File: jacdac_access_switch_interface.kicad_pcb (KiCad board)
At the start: 2 copper layers, 25 x 25 mm, 23 parts, among them J1 Conn_Jacdac_CardEdge, J2 54-00036_audio_plug, J3 Conn_HackConnect, U1 NCP114ASN330T1G, U2 STM32G031J6M6, U3 AQY282

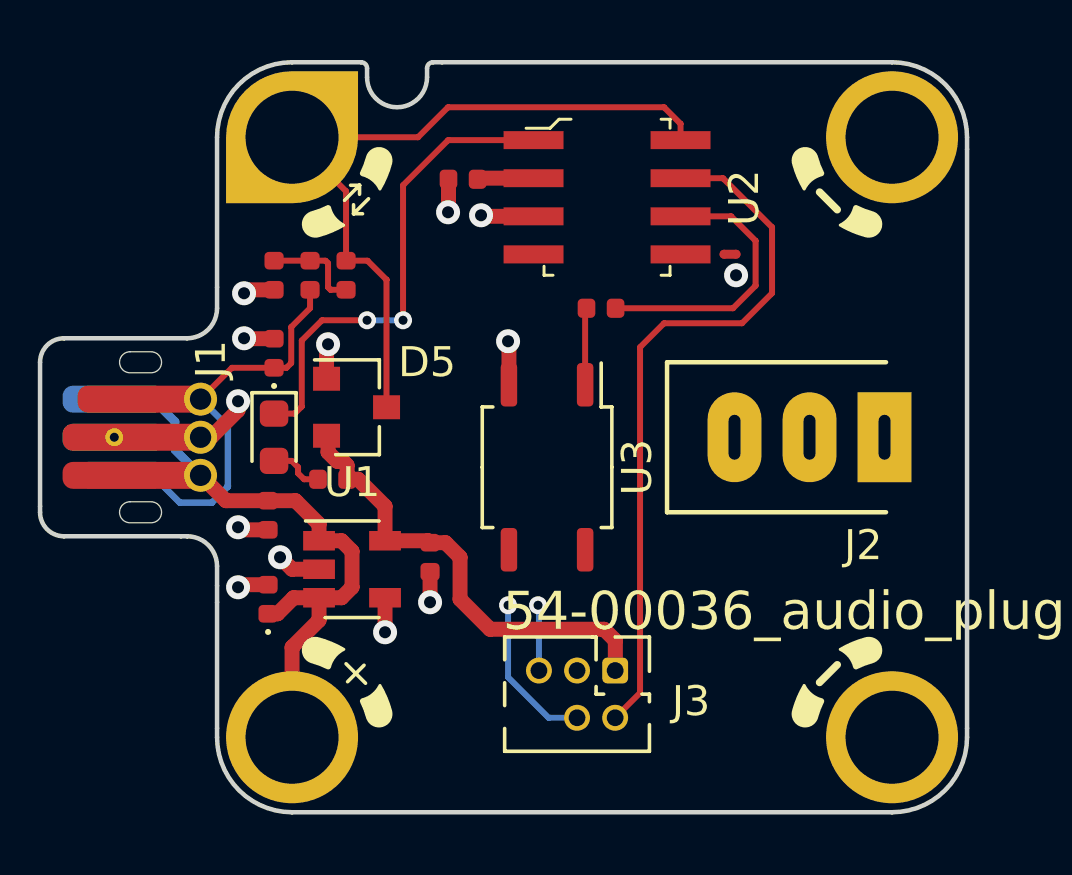
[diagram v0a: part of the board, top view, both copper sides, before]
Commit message: Added 3dshapes and updated PCB
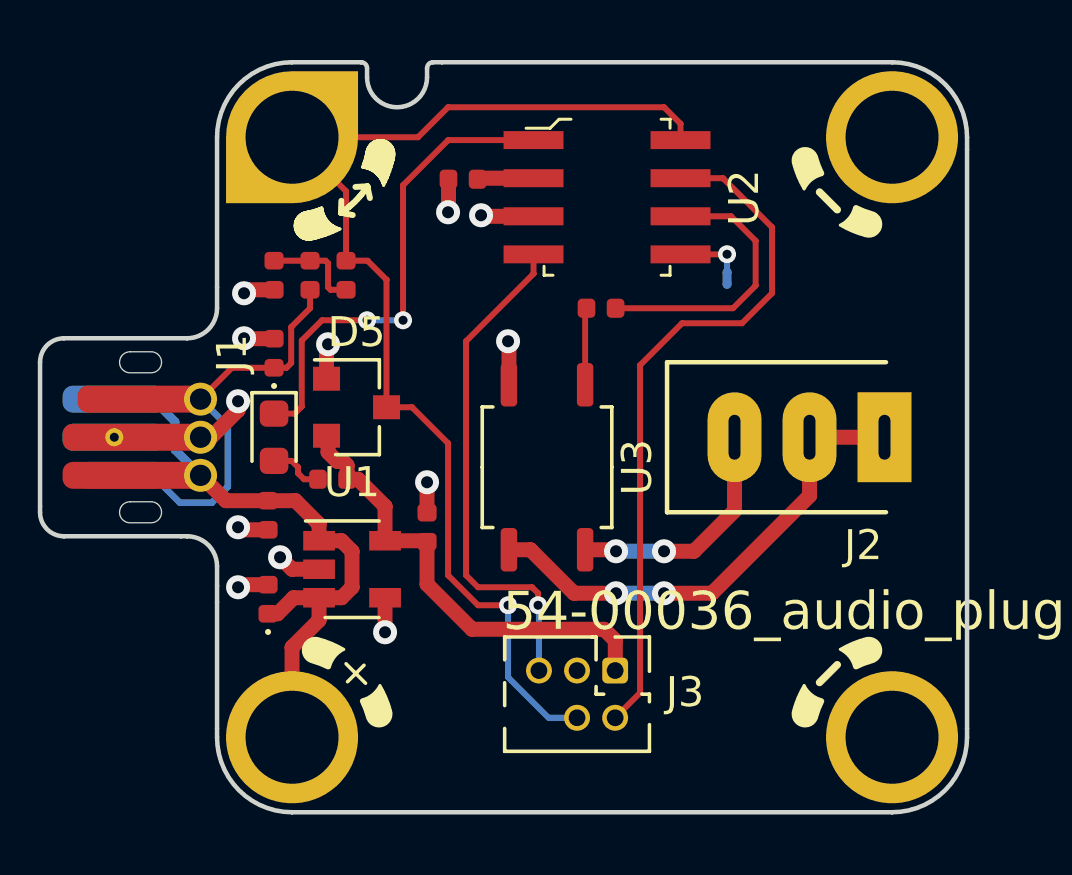
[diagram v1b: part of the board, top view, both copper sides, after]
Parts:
- NT1: moved to B.Cu
- U3: footprint Package_SO:SOP-4_3.8x4.1mm_P2.54mm -> jacdac_access_switch_interface:SOP-4_3.8x4.1mm_P2.54mm
- moved C4 1.00 mm to (154.5, 93.0), turned to 90 degrees
- moved NT1 0.81 mm to (164.5, 84.7), turned to 90 degrees
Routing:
- net /SLEEVE: track 0.00 -> 16.4 mm, vias 0 -> 2
- net /nRESET: track 2.19 -> 16.9 mm
- net /JD_DATA_MCU_SWCLK: track 30.1 -> 39.5 mm
- net /PLUG_TIP: track 0.00 -> 8.30 mm, vias 0 -> 2
- net Net-(U2-PA8/PA11[PA9]/PB0/PB1): track 0.00 -> 2.15 mm, vias 0 -> 1
- net GND: vias 13 -> 12

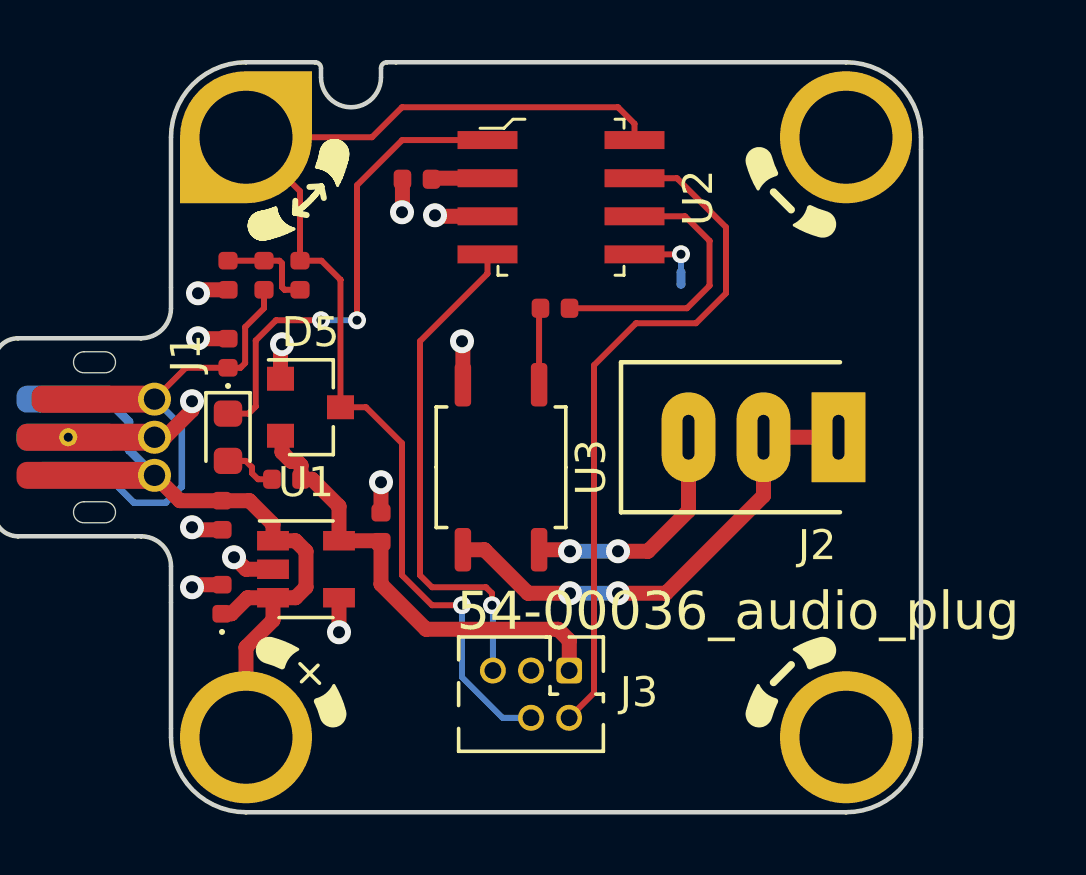
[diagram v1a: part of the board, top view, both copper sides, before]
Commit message: v1.2 almost routed. Found error in connector placement.
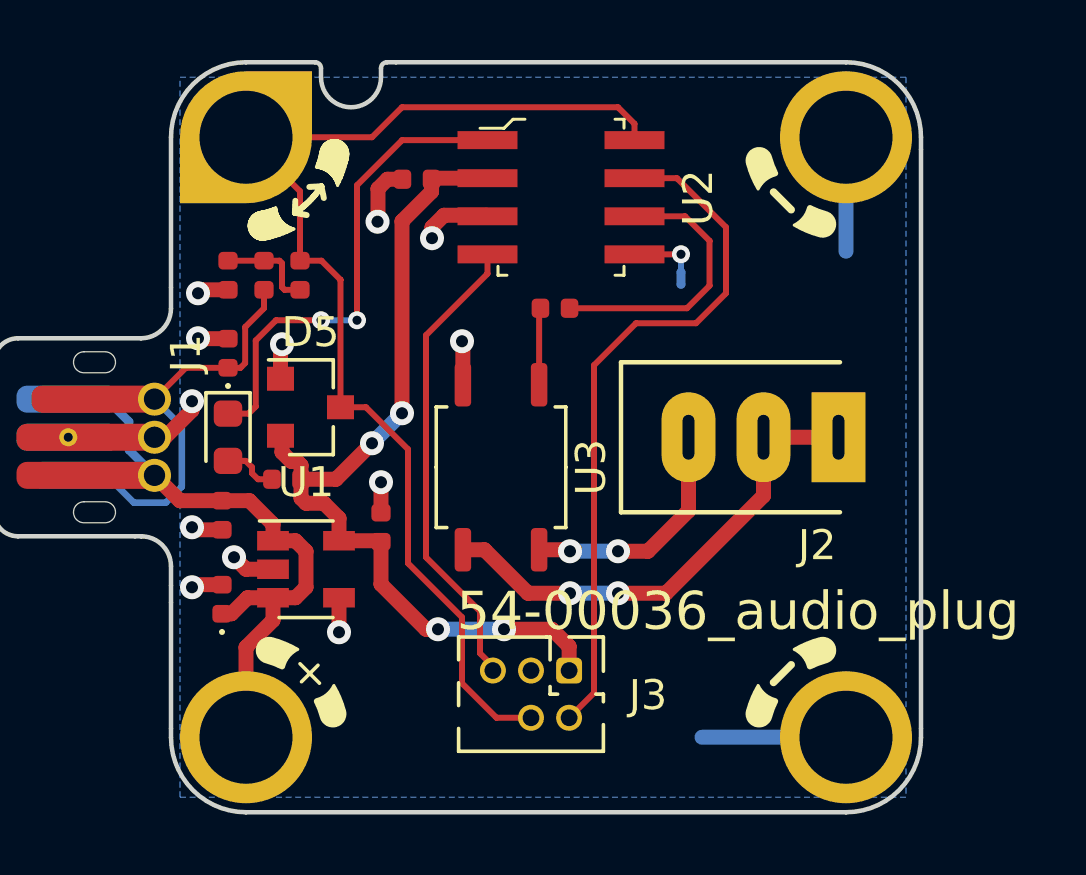
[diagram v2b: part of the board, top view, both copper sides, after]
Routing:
- net +3V3: track 17.4 -> 29.9 mm, vias 0 -> 4
- net GND: track 15.2 -> 25.3 mm
- net JD_PWR: track 17.1 -> 15.8 mm
- net /nRESET: track 16.9 -> 15.6 mm, vias 1 -> 0
- net /JD_DATA_MCU_SWCLK: track 39.5 -> 39.0 mm, vias 1 -> 0
- added copper zone on B.Cu, net GND

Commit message: v1.3 started, board outline complete
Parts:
- removed MH2A1: MountingHole_Pad, Jacdac:jacdac_hole_GND_MH2A
- removed MH2B1: MountingHole_Pad, Jacdac:jacdac_hole_GND_MH2B
- added MH2: jacdac_hole_GND_MH2, Jacdac:jacdac_hole_GND_MH2, F.Cu at (170.0, 70.0)
- added MH4: jacdac_hole_GND_MH4, Jacdac:jacdac_hole_GND_MH4, F.Cu at (170.0, 100.0)
- U3: footprint jacdac_access_switch_interface:SOP-4_3.8x4.1mm_P2.54mm -> Package_SO:SOP-4_3.8x4.1mm_P2.54mm
- moved J2 20.2 mm to (196.1, 90.0)
- moved C3 10.2 mm to (156.9, 71.3)
- moved R3 10.2 mm to (161.5, 75.6)
- moved U2 10.2 mm to (161.7, 71.9)
- moved NT1 10.1 mm to (163.6, 74.6)
- moved U3 10.1 mm to (168.5, 89.5)
- moved MH1 10.0 mm to (150.0, 70.0)
- moved FB1 8.08 mm to (154.8, 77.7)
- moved C1 8.08 mm to (153.6, 77.7)
- moved R1 8.08 mm to (156.0, 77.7)
- moved C4 7.14 mm to (161.5, 91.6)
- moved D5 7.14 mm to (159.2, 87.6)
- moved U1 7.14 mm to (159.0, 93.0)
- moved J1 6.66 mm to (150.0, 85.0)
- moved R2 5.87 mm to (157.1, 90.0)
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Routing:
- net /JD_DATA_MCU_SWCLK: track 39.0 -> 0.00 mm
- net +3V3: track 29.9 -> 0.00 mm, vias 4 -> 1
- net GND: track 25.3 -> 0.00 mm, vias 12 -> 8
- net /SWDIO: track 23.4 -> 0.00 mm
- net /SLEEVE: track 16.4 -> 0.00 mm, vias 2 -> 0
- net /JD_STATUS: track 16.4 -> 0.00 mm
- net JD_PWR: track 15.8 -> 0.00 mm
- net /nRESET: track 15.6 -> 0.00 mm
- net /SWITCH: track 9.31 -> 0.00 mm
- net /PLUG_TIP: track 8.30 -> 0.00 mm, vias 2 -> 0
- net /JD_DATA: track 8.05 -> 0.00 mm
- net Net-(C1-Pad1): track 3.27 -> 0.00 mm
- net Net-(R3-Pad1): track 2.57 -> 0.00 mm
- net Net-(U2-PA8/PA11[PA9]/PB0/PB1): track 2.15 -> 0.00 mm
- net Net-(D6-A): track 1.84 -> 0.00 mm
- removed copper zone on B.Cu, net GND
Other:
- board size 25 x 25 mm -> 25 x 35 mm
- board text added: "Switch output v1.3"
- board text removed: "Switch output v1.2"

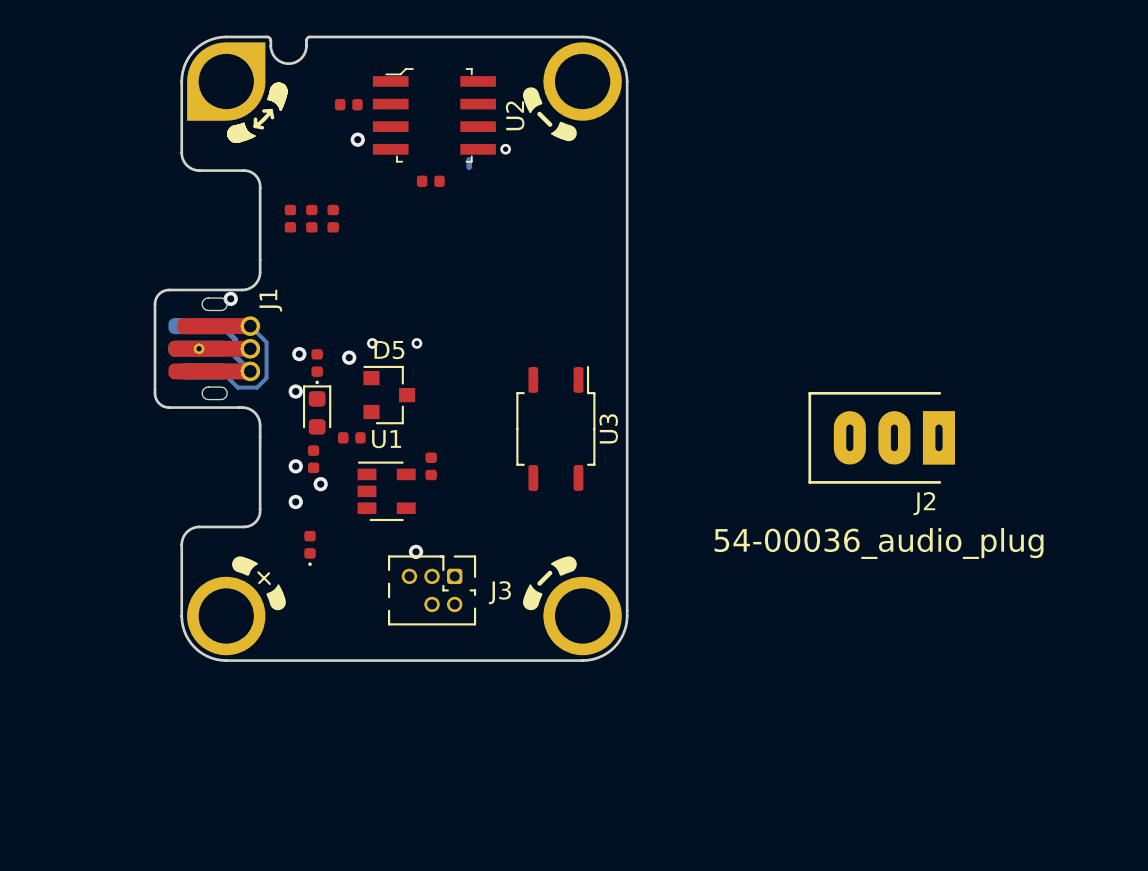
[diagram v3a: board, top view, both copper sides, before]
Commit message: Replaced 3.5mm plug with 2x3.5mm sockets on schematic
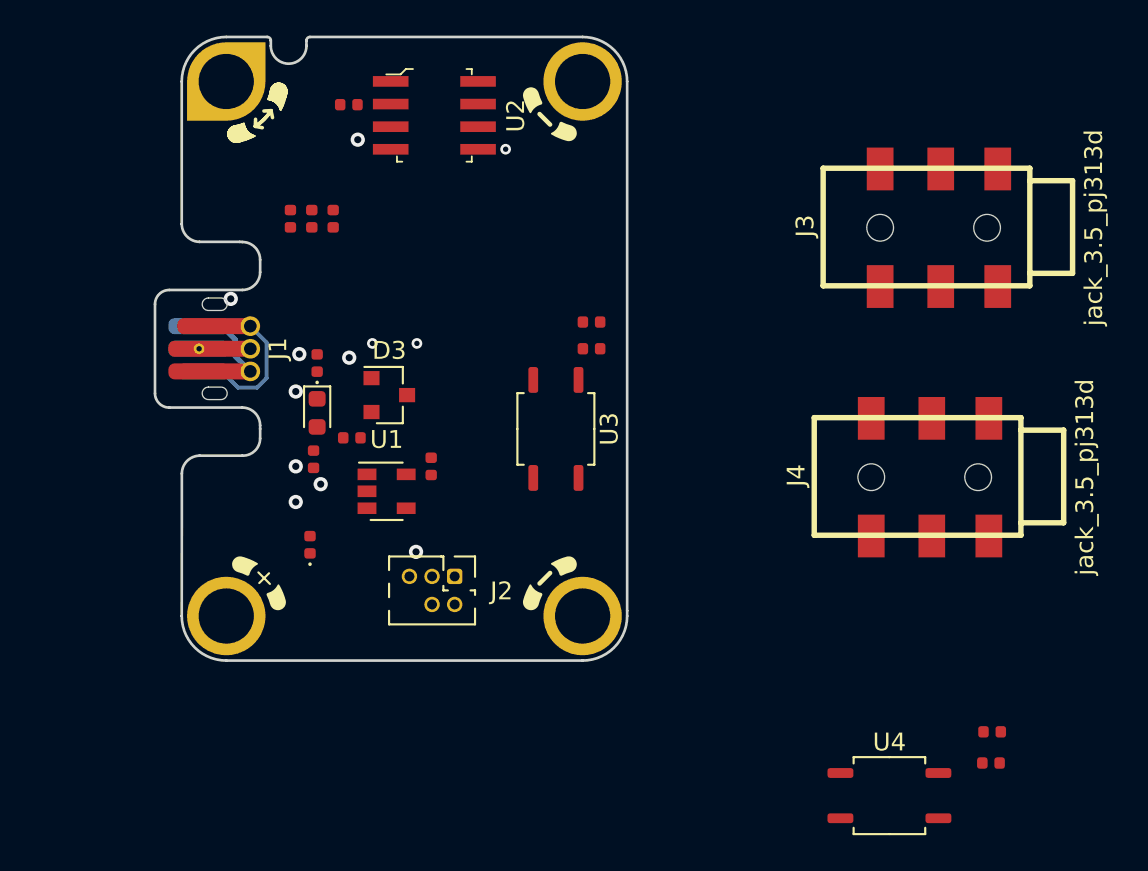
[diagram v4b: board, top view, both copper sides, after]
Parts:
- removed the J2 at (196.1, 90.0)
- removed NT1: NetTie_2, jacdac_access_switch_interface:NetTie-2_SMD_Pad0.3mm
- added J3: jack_3.5_pj313d, jacdac_access_switch_interface:jack_3.5_pj313d_smt, F.Cu at (192.7, 80.5)
- added J4: jack_3.5_pj313d, jacdac_access_switch_interface:jack_3.5_pj313d_smt, F.Cu at (192.2, 94.5)
- added R2: 130, jacdac_access_switch_interface:R_0402_1005Metric, F.Cu at (170.5, 83.5)
- added R5: 130, jacdac_access_switch_interface:R_0402_1005Metric, F.Cu at (192.9, 108.2)
- added R6: 220, jacdac_access_switch_interface:R_0402_1005Metric, F.Cu at (193.0, 106.5)
- added U4: AQY282, jacdac_access_switch_interface:SOP-4_3.8x4.1mm_P2.54mm, F.Cu at (187.2, 110.1)
- J1: footprint Jacdac:JD-PEC-02_Prerouted -> Jacdac:JD-PEC-02_Prerouted_recessed
- MH2: value jacdac_hole_GND_MH2 -> Val**
- MH4: value jacdac_hole_GND_MH4 -> Val**
- R3: value 330 -> 220
- U3: footprint Package_SO:SOP-4_3.8x4.1mm_P2.54mm -> jacdac_access_switch_interface:SOP-4_3.8x4.1mm_P2.54mm
- moved R3 13.0 mm to (170.5, 85.0), turned to 180 degrees
- renumbered C2 to C1, C4 to C2, C1 to C3, C3 to C4, D3 to D1, D4 to D2, D5 to D3, D6 to D4, J3 to J2, R2 to R4
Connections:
- R3 pad 2: /SWITCH -> Net-(R2-Pad1)
- U2 pad 5: Net-(U2-PA8/PA11[PA9]/PB0/PB1) -> /SWITCH2
- U2 pad 6: /SWITCH -> /SWITCH1
- U3 pad 3: /SLEEVE -> /SLEEVE1
- U3 pad 4: /PLUG_TIP -> /PLUG_TIP1
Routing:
- net Net-(U2-PA8/PA11[PA9]/PB0/PB1): vias 1 -> 0
- net /SWITCH2: vias 0 -> 1
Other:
- outline, holes or cut-outs redrawn

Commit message: Component placement for 30x30 board
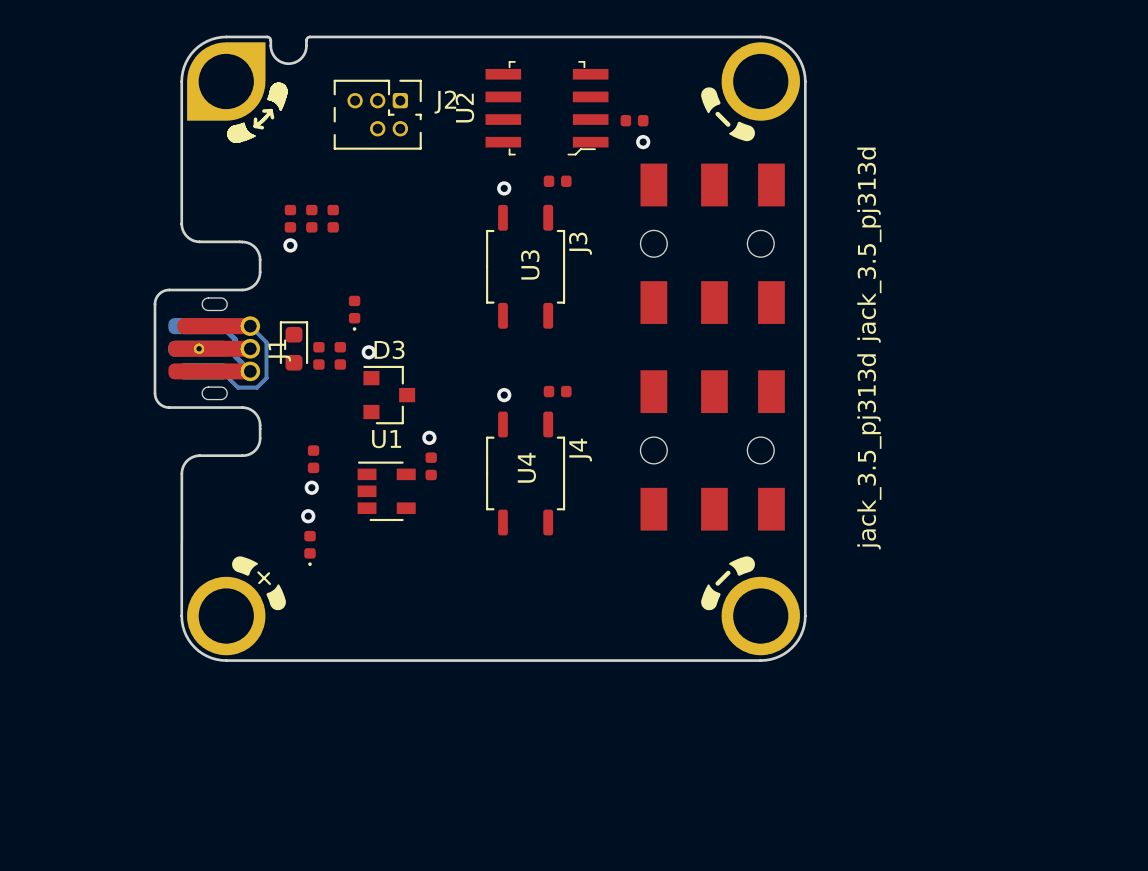
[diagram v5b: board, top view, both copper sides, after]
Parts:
- removed the R2 at (170.5, 83.5)
- R2: renamed from R3; value 220 -> 330
- R3: renamed from R6; value 220 -> 330
- R4: value 130 -> 330
- R5: value 130 -> 220
- moved R5 43.1 mm to (156.4, 85.4), turned to -90 degrees
- moved R3 31.0 mm to (168.6, 87.4)
- moved U4 27.3 mm to (166.8, 92.0), turned to -90 degrees
- moved J2 26.9 mm to (159.8, 71.9)
- moved C4 16.1 mm to (172.9, 72.2), turned to 0 degrees
- moved J3 12.7 mm to (180.0, 81.4)
- moved J4 12.3 mm to (180.0, 93.0)
- moved MH2 10.0 mm to (180.0, 70.0)
- moved MH4 10.0 mm to (180.0, 100.0)
- moved R2 9.59 mm to (168.6, 75.6), turned to 0 degrees
- moved U3 9.26 mm to (166.8, 80.4)
- moved U2 6.33 mm to (168.0, 71.5), turned to 90 degrees
- moved R4 4.96 mm to (155.2, 85.4), turned to -90 degrees
- moved D4 3.83 mm to (153.8, 85.0)
- moved D1 3.66 mm to (157.2, 82.8)
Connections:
- MH2 pad MH2: (no net) -> GND
- MH4 pad MH4: (no net) -> GND
- R2 pad 2: Net-(R2-Pad1) (its old number) -> /SWITCH1
- R3 pad 2: Net-(R5-Pad1) -> /SWITCH2
- R5 pad 1: Net-(R5-Pad1) -> +3V3
- R5 pad 2: /SWITCH2 -> Net-(D4-A)
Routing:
- net /SWITCH2: vias 1 -> 0
- net /JD_STATUS: vias 2 -> 0
- net +3V3: vias 1 -> 0
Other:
- board size 25 x 35 mm -> 35 x 35 mm

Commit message: Laying out 20x30mm board
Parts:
- moved C4 14.2 mm to (159.0, 74.8)
- moved R3 13.3 mm to (158.8, 96.4), turned to 180 degrees
- moved R2 12.2 mm to (156.4, 74.8), turned to 180 degrees
- moved J3 10.1 mm to (170.0, 83.0)
- moved J4 10.0 mm to (170.0, 93.4)
- moved MH2 10.0 mm to (170.0, 70.0)
- moved MH4 10.0 mm to (170.0, 100.0)
- moved U3 9.43 mm to (157.4, 79.6)
- moved U4 8.96 mm to (162.4, 99.8), turned to 0 degrees
- moved C2 8.01 mm to (156.2, 97.6), turned to 180 degrees
- moved U1 7.96 mm to (155.6, 100.2)
- moved D3 7.77 mm to (155.4, 94.4)
- moved R1 5.91 mm to (150.4, 75.8), turned to 90 degrees
- moved C1 5.52 mm to (150.8, 94.9), turned to 90 degrees
- moved D2 5.41 mm to (149.4, 94.9)
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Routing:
- net GND: vias 8 -> 7
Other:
- board size 35 x 35 mm -> 25 x 35 mm
